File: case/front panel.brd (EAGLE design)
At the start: 165 x 30.1 mm, 5 parts

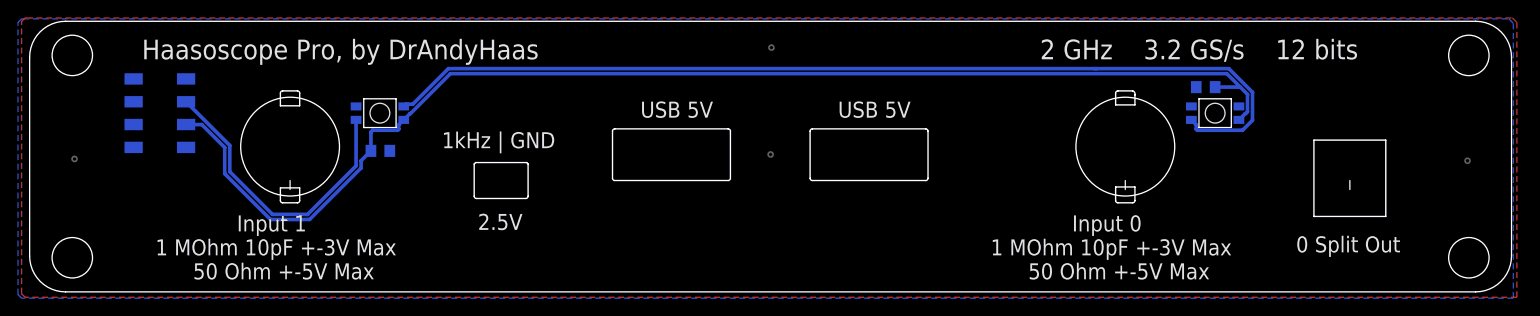
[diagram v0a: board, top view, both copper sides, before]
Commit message: add light pipe holes and remove leds
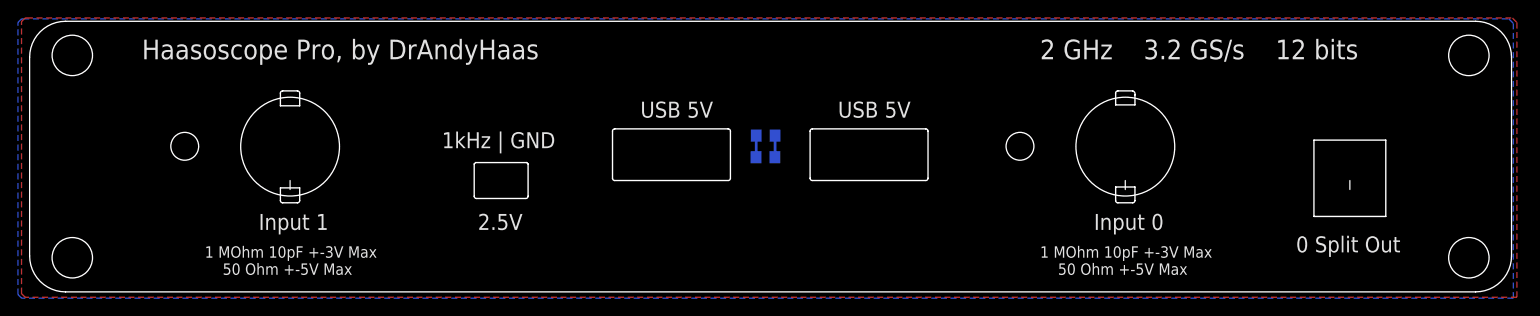
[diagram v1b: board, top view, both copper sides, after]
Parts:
- removed JP1: connect, pinhead+:2X04_SMT
- removed LED0, LED1: WS2812B_SK6812E, microbuilder:NEO3535_REVERSE
- moved C2 49.3 mm to (79.4, 17.5)
- moved C1 42.8 mm to (79.4, 15.1), turned to 0 degrees
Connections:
- removed net DIN: JP1.3, LED1.4-DIN
- removed net N$2: LED0.4-DIN, LED1.2-DOUT
- net 5V: no longer JP1.5, LED0.1-VDD, LED1.1-VDD
- net GND: no longer JP1.1, JP1.2, JP1.4, JP1.6, JP1.7, JP1.8, LED0.3-GND, LED1.3-GND
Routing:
- net 5V: track 140.0 -> 2.41 mm
- net N$2: track 108.5 -> 0.00 mm
- net DIN: track 33.2 -> 0.00 mm
- net GND: track 0.00 -> 2.41 mm, vias 4 -> 0
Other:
- board text added: "1 MOhm 10pF +-3V Max 50 Ohm +-5V Max"
- board text added: "13mm from center of bnc to left gnd hole center 11.73mm from center of bnc to center of pipe Hole center should be 3.81mm from top of board and 3mm in diameter"
- board text added: "Input 0"
- board text added: "Input 1"
- board text removed: "5V"
- board text removed: "DIN"
- board text removed: "GND"
- board text removed: "Input 0 1 MOhm 10pF +-3V Max 50 Ohm +-5V Max"
- board text removed: "Input 1 1 MOhm 10pF +-3V Max 50 Ohm +-5V Max"

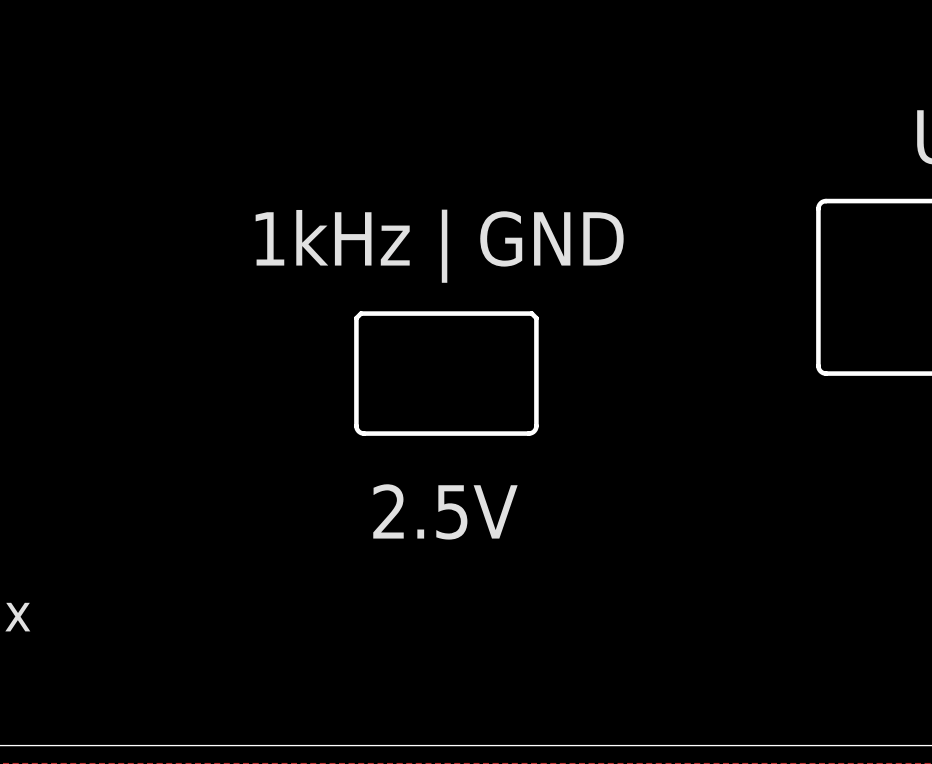
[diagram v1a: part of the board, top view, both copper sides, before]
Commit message: add 1kHzout and gnd tabs and cutouts on front panel
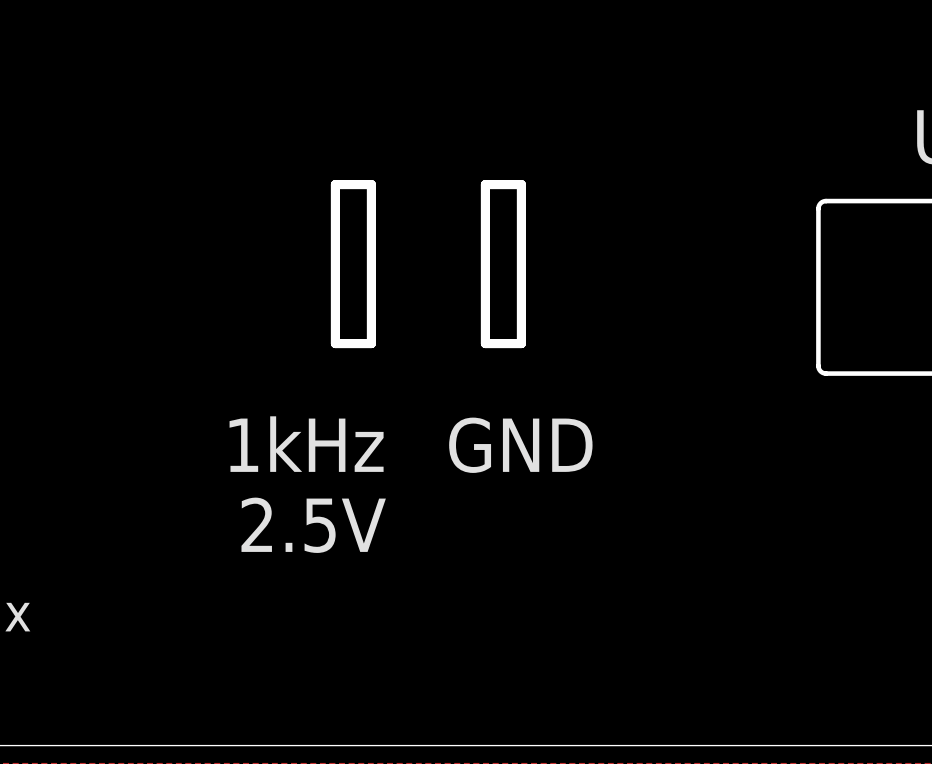
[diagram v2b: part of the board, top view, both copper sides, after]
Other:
- outline, holes or cut-outs redrawn
- board text added: "1kHz 2.5V"
- board text added: "GND"
- board text removed: "1kHz | GND"
- board text removed: "2.5V"
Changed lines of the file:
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@@
 <wire x1="140.5" y1="17" x2="148.5" y2="17" width="0.1524" layer="20"/>
 <wire x1="148.5" y1="17" x2="148.5" y2="8.5" width="0.1524" layer="20"/>
-<wire x1="53" y1="10.754" x2="53" y2="14.346" width="0.1524" layer="20"/>
-<wire x1="53" y1="14.346" x2="52.846" y2="14.5" width="0.1524" layer="20"/>
-<wire x1="52.846" y1="14.5" x2="47.154" y2="14.5" width="0.1524" layer="20"/>
-<wire x1="47.154" y1="14.5" x2="47" y2="14.346" width="0.1524" layer="20"/>
-<wire x1="47" y1="14.346" x2="47" y2="10.754" width="0.1524" layer="20"/>
-<wire x1="47" y1="10.754" x2="47.254" y2="10.5" width="0.1524" layer="20" curve="90"/>
-<wire x1="47.254" y1="10.5" x2="52.746" y2="10.5" width="0.1524" layer="20"/>
-<wire x1="52.746" y1="10.5" x2="53" y2="10.754" width="0.1524" layer="20" curve="90"/>
-<text x="43.4" y="16.1" size="1.778" layer="21" font="vector">1kHz | GND</text>
-<text x="47.4" y="7" size="1.778" layer="21" font="vector">2.5V</text>
+<text x="48" y="11" size="1.778" layer="21" font="vector" rot="R180">1kHz
+2.5V</text>
+<text x="55" y="11" size="1.778" layer="21" font="vector" rot="R180">GND</text>
 <text x="3" y="19.7" size="0.4064" layer="27">13mm from center of bnc to left gnd hole center
 11.73mm from center of bnc to center of pipe
@@
 <text x="110" y="2" size="1.27" layer="21" font="vector">1 MOhm 10pF +-3V Max
     50 Ohm +-5V Max</text>
+<wire x1="46.9" y1="13.6" x2="46.9" y2="18.6" width="0.1524" layer="22"/>
+<wire x1="51.9" y1="13.6" x2="51.9" y2="18.6" width="0.1524" layer="22"/>
+<wire x1="46.3" y1="13.5" x2="47.5" y2="13.5" width="0.3048" layer="20"/>
+<wire x1="47.5" y1="13.5" x2="47.5" y2="18.8" width="0.3048" layer="20"/>
+<wire x1="47.5" y1="18.8" x2="46.3" y2="18.8" width="0.3048" layer="20"/>
+<wire x1="46.3" y1="18.8" x2="46.3" y2="13.5" width="0.3048" layer="20"/>
+<wire x1="51.3" y1="13.5" x2="52.5" y2="13.5" width="0.3048" layer="20"/>
+<wire x1="52.5" y1="13.5" x2="52.5" y2="18.8" width="0.3048" layer="20"/>
+<wire x1="52.5" y1="18.8" x2="51.3" y2="18.8" width="0.3048" layer="20"/>
+<wire x1="51.3" y1="18.8" x2="51.3" y2="13.5" width="0.3048" layer="20"/>
 </plain>
 <attributes>

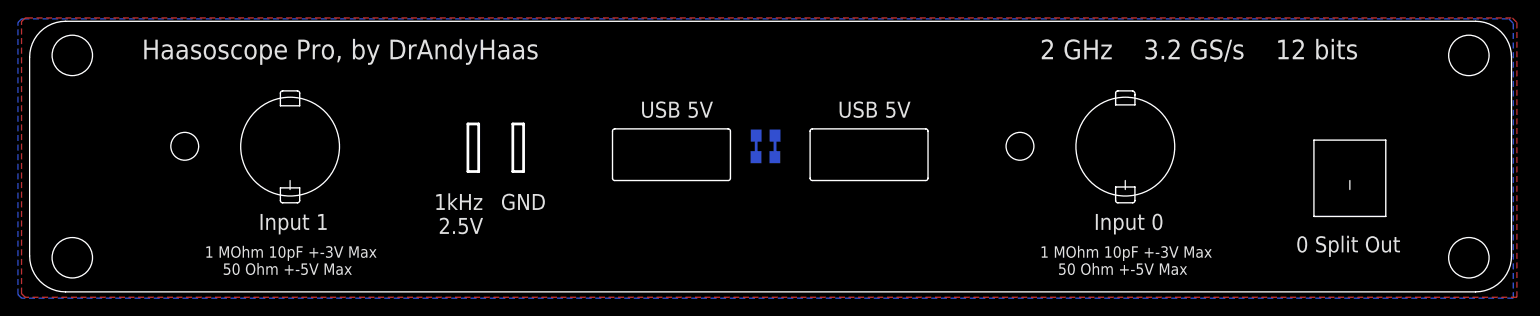
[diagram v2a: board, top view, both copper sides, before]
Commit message: add gnd near screw holes
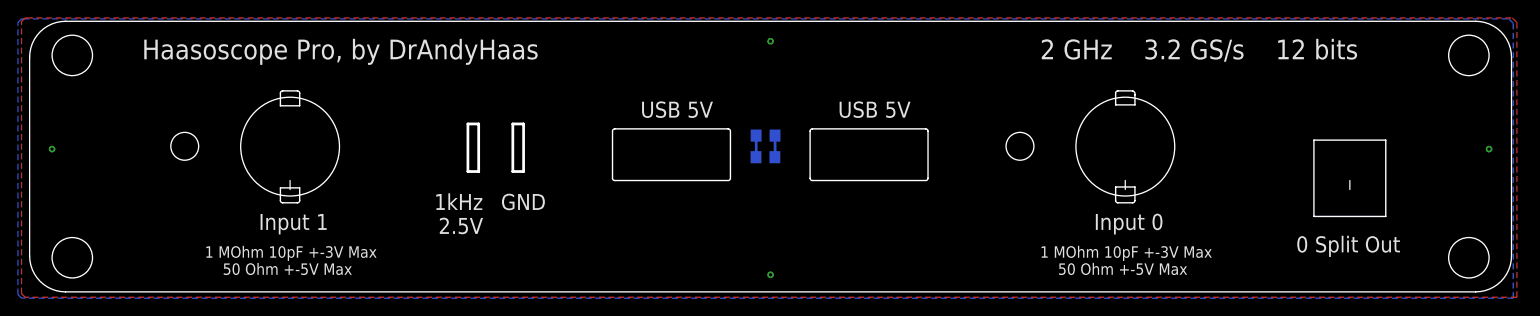
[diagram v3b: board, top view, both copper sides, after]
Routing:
- net GND: vias 0 -> 4
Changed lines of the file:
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@@
 2.5V</text>
 <text x="55" y="11" size="1.778" layer="21" font="vector" rot="R180">GND</text>
-<text x="3" y="19.7" size="0.4064" layer="27">13mm from center of bnc to left gnd hole center
+<text x="5.7" y="18.2" size="0.4064" layer="27">13mm from center of bnc to left gnd hole center
 11.73mm from center of bnc to center of pipe
-Hole center should be 3.81mm from top of board and 3mm in diameter</text>
+Hole center should be 3.81mm from top of board
+and 3mm in diameter</text>
 <hole x="14.77" y="16.31" drill="3.1"/>
 <hole x="107.77" y="16.31" drill="3.1"/>
@@
 <wire x1="52.5" y1="18.8" x2="51.3" y2="18.8" width="0.3048" layer="20"/>
 <wire x1="51.3" y1="18.8" x2="51.3" y2="13.5" width="0.3048" layer="20"/>
+<polygon width="0.1524" layer="29">
+<vertex x="6.5" y="31.4"/>
+<vertex x="-4.5" y="31.4"/>
+<vertex x="-4.5" y="21.9"/>
+<vertex x="6.5" y="21.9"/>
+</polygon>
+<polygon width="0.1524" layer="31">
+<vertex x="6.5" y="31.3"/>
+<vertex x="-4.4" y="31.3"/>
+<vertex x="-4.4" y="22"/>
+<vertex x="6.5" y="22"/>
+</polygon>
+<polygon width="0.1524" layer="29">
+<vertex x="6.5" y="8.1"/>
+<vertex x="-4.6" y="8.1"/>
+<vertex x="-4.6" y="-1.4"/>
+<vertex x="6.5" y="-1.4"/>
+</polygon>
+<polygon width="0.1524" layer="31">
+<vertex x="6.5" y="8"/>
+<vertex x="-4.5" y="8"/>
+<vertex x="-4.5" y="-1.3"/>
+<vertex x="6.5" y="-1.3"/>
+</polygon>
+<polygon width="0.1524" layer="29">
+<vertex x="164.3" y="31.4"/>
+<vertex x="153.3" y="31.4"/>
+<vertex x="153.3" y="21.9"/>
+<vertex x="164.3" y="21.9"/>
+</polygon>
+<polygon width="0.1524" layer="31">
+<vertex x="164.3" y="31.3"/>
+<vertex x="153.4" y="31.3"/>
+<vertex x="153.4" y="22"/>
+<vertex x="164.3" y="22"/>
+</polygon>
+<polygon width="0.1524" layer="29">
+<vertex x="164.3" y="8"/>
+<vertex x="153.3" y="8"/>
+<vertex x="153.3" y="-1.5"/>
+<vertex x="164.3" y="-1.5"/>
+</polygon>
+<polygon width="0.1524" layer="31">
+<vertex x="164.3" y="7.9"/>
+<vertex x="153.4" y="7.9"/>
+<vertex x="153.4" y="-1.4"/>
+<vertex x="164.3" y="-1.4"/>
+</polygon>
 </plain>
 <attributes>
@@
 <wire x1="78.4" y1="17.5" x2="78.4" y2="15.12" width="0.3048" layer="16"/>
 <wire x1="78.4" y1="15.12" x2="78.38" y2="15.1" width="0.3048" layer="16"/>
+<via x="0" y="16" extent="1-16" drill="0.35"/>
+<via x="80" y="2" extent="1-16" drill="0.35"/>
+<via x="80" y="28" extent="1-16" drill="0.35"/>
+<via x="160" y="16" extent="1-16" drill="0.35"/>
 </signal>
 <signal name="5V">
